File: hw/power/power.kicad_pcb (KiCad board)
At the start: 4 copper layers, 83.1 x 46.9 mm, 51 parts, among them J1 MSTB2,5/3-GF-5,08_1776511, J2 Conn_02x06, Q1 BSP315P, U1 LM5122, U2 TPS54560, U3 AMS1117-3.3

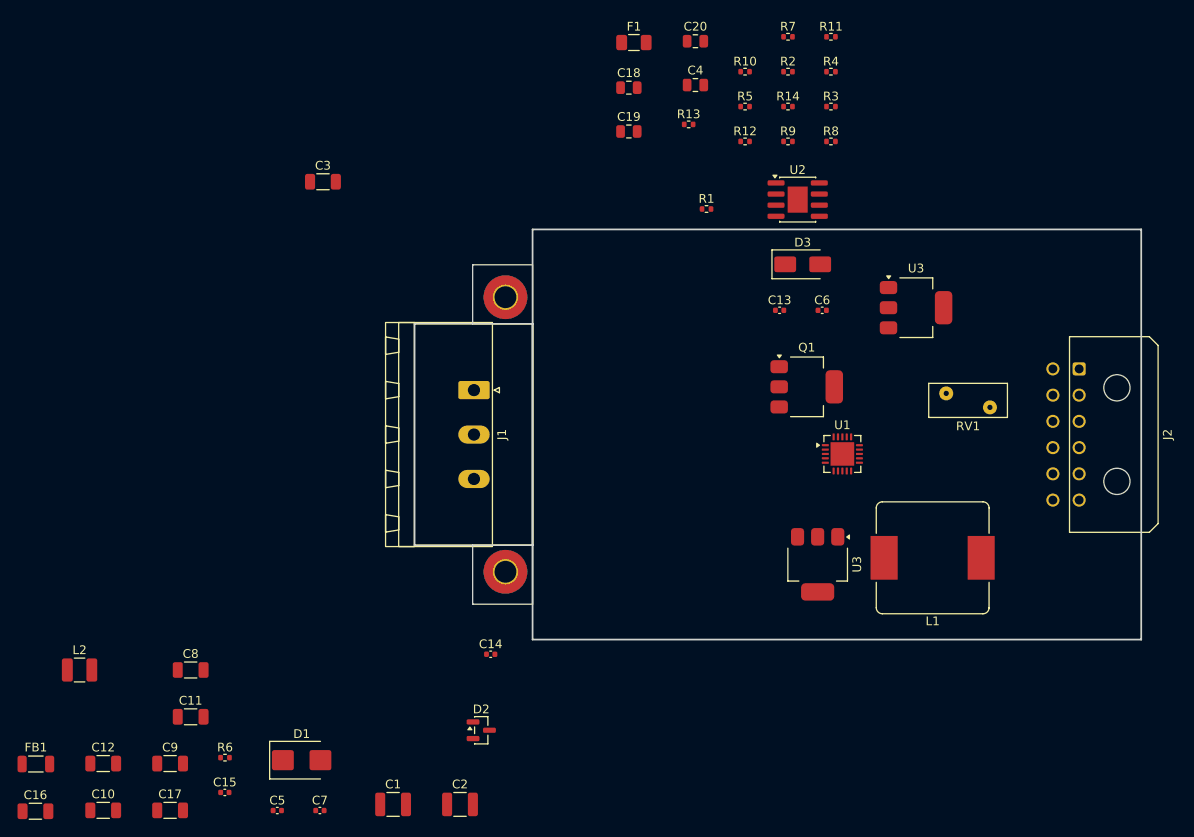
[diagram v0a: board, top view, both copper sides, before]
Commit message: s5: digital/power split, Mini-Fit interconnect, front-panel light guide
Land the board split and everything that followed from it:

- Move all switching (input protection, LM5122 boost, TPS54560 buck,
  3V3 LDO) to the power board; the core board receives finished rails.
- Board-to-board interconnect reduced to 8 pins: VBUS x2 + GND x2 +
  VIN_24V + VDD_5V + VDD_3V3 + MAIN_EN. Core J9 = Molex Mini-Fit Jr
  5569-08A1 2x4 right-angle header (serviceable, unplugs); power J2 =
  8-hole solder field (16AWG stripped ends, 1.7mm drill). Mate is an
  off-the-shelf Mini-Fit Versa 16AWG/9A cable assembly. Pin->net maps
  verified identical between the two boards.
- Front-panel status: Mentor 1278.1004 4-way bargraph light guide with
  Osram Mini TOPLED LEDs (green/yellow/orange/red), driven from the
  STM32 supervisor with PWM breathing; frees T113 PB7/PE4.
- PE: power-board input earth bonded to 4x M3_PE chassis mounting
  holes; the single GND<->PE bond stays on the core board.
- New footprints (light guide, Osram LED, 8-way solder field),
  per-board fp-lib-tables, and local vendor-3d models (${KIPRJMOD}).
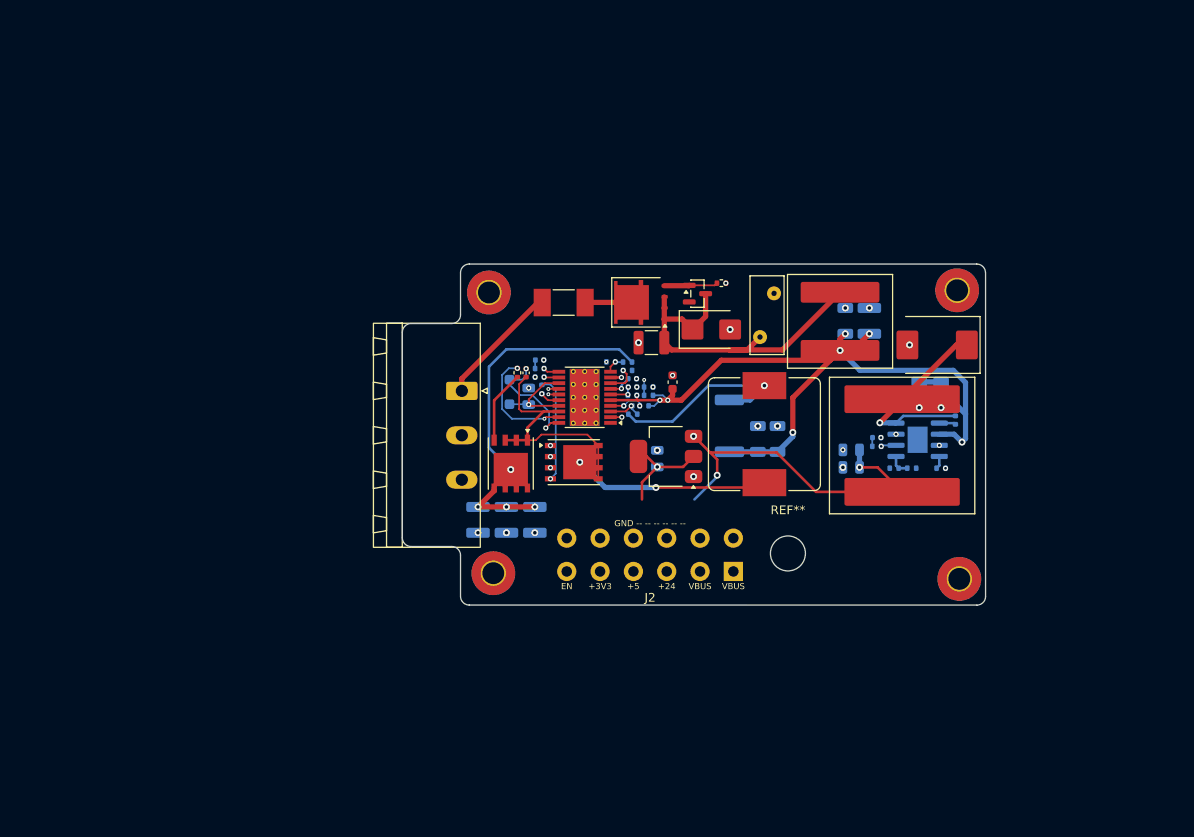
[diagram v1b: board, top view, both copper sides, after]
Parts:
- removed the J1 at (114.4, 90.7)
- removed the U3 at (164.9, 81.3)
- removed the U3 at (153.7, 110.7)
- added C21: 10uF, Capacitor_SMD:C_0805_2012Metric, B.Cu at (135.4, 98.6)
- added D4: PMEG10010ELR-QX, Diode_SMD:D_SOD-123F, B.Cu at (118.5, 90.9)
- added L1: 22uH, Inductor_SMD:L_Bourns_SRP1245A, F.Cu at (147.6, 95.8)
- added PWR_MH3: MountingHole_2.5mm_Pad_TopBottom, MountingHole:MountingHole_2.5mm_Pad_TopBottom, F.Cu at (169.7, 79.3)
- added PWR_MH4: MountingHole_2.5mm_Pad_TopBottom, MountingHole:MountingHole_2.5mm_Pad_TopBottom, F.Cu at (169.9, 112.3)
- added Q2: BSC057N08NS3G, Package_SO:PowerPAK_SO-8_Single, F.Cu at (125.8, 99.0)
- added Q3: BSC057N08NS3G, Package_SO:PowerPAK_SO-8_Single, F.Cu at (118.6, 99.1)
- added R15: 100k, Resistor_SMD:R_0402_1005Metric, B.Cu at (167.8, 99.7)
- added R16: 24.9k, Resistor_SMD:R_0402_1005Metric, B.Cu at (160.5, 97.2)
- added R17: 52.3k, Resistor_SMD:R_0402_1005Metric, B.Cu at (162.5, 99.7)
- added R18: 10k, Resistor_SMD:R_0402_1005Metric, B.Cu at (164.5, 99.7)
- added REF**: MountingHole_4mm, MountingHole:MountingHole_4mm, F.Cu at (150.3, 109.4)
- added RS: R_5m_2W, Resistor_SMD:R_2512_6332Metric, B.Cu at (143.6, 94.8)
- added U3: AMS1117-3.3, Package_TO_SOT_SMD:SOT-223-3_TabPin2, F.Cu at (136.4, 98.3)
- C10: value 10uF -> 10uF/100V; footprint Capacitor_SMD:C_1206_3216Metric -> Capacitor_SMD:C_1210_3225Metric; moved to B.Cu
- C11, C12: value 22uF -> 10uF/100V; footprint Capacitor_SMD:C_1206_3216Metric -> Capacitor_SMD:C_1210_3225Metric; moved to B.Cu
- C13, C14: value 100nF -> 22uF/63V; footprint Capacitor_SMD:C_0402_1005Metric -> Capacitor_SMD:C_1206_3216Metric; moved to B.Cu
- C15: value 15nF -> 100nF; moved to B.Cu
- C16: value 2.2uF -> 15nF; footprint Capacitor_SMD:C_1206_3216Metric -> Capacitor_SMD:C_0402_1005Metric; moved to B.Cu
- C17, C19, C2, C3, C6, C7, R7, U2: moved to B.Cu
- C18: value 22uF -> 2.2uF; footprint Capacitor_SMD:C_0805_2012Metric -> Capacitor_SMD:C_1206_3216Metric; moved to B.Cu
- C20: value 10uF -> 22uF; moved to B.Cu
- C4: value 4.7uF -> 1uF; footprint Capacitor_SMD:C_0805_2012Metric -> Capacitor_SMD:C_0603_1608Metric
- C5: value 100nF -> 4.7uF; footprint Capacitor_SMD:C_0402_1005Metric -> Capacitor_SMD:C_0805_2012Metric; moved to B.Cu
- C8: value 10uF -> 100pF; footprint Capacitor_SMD:C_1206_3216Metric -> Capacitor_SMD:C_0402_1005Metric; moved to B.Cu
- C9: value 10uF -> 100nF; footprint Capacitor_SMD:C_1206_3216Metric -> Capacitor_SMD:C_0402_1005Metric
- D1: value SMBJ30A -> SMBJ33A
- D3: value SS54 -> SS56; footprint Diode_SMD:D_SMA -> Diode_SMD:D_SMC
- F1: value Fuse_2A_TL -> Fuse_12A_TL_0452012; footprint Fuse:Fuse_1206_3216Metric -> Fuse:Fuse_Littelfuse-NANO2-451_453
- FB1: value BLM31PG601SN1 -> 2.2uH XAL1010-222MED Isat34A DCR2.8mR (LCSC C5125746); footprint Inductor_SMD:L_1206_3216Metric -> Inductor_SMD:L_Coilcraft_XAL1010-XXX
- J1: renamed from L1; value 22uH -> MSTB2,5/3-GF-5,08_1776511; footprint Inductor_SMD:L_Bourns_SRP1245A -> Connector_Phoenix_MSTB:PhoenixContact_MSTB_2,5_3-GF-5,08_1x03_P5.08mm_Horizontal_ThreadedFlange
- J2: value Conn_02x06 -> PowerCable_12way; footprint Connector_Molex:Molex_Micro-Fit_3.0_43045-1200_2x06_P3.00mm_Horizontal -> power:PowerCable_12way_SolderField
- L2: footprint Inductor_SMD:L_1210_3225Metric -> Inductor_SMD:L_Coilcraft_XAL1510-333
- Q1: value BSP315P -> SQJ409EP P-ch 40V 7mR (LCSC C727776); footprint Package_TO_SOT_SMD:SOT-223-3_TabPin2 -> Package_SO:PowerPAK_SO-8L_Single
- R10, R9: value 100k -> 100R; moved to B.Cu
- R11: value 13k -> 2.2R; moved to B.Cu
- R12: value 24.9k -> 2.2R
- R13: value 52.3k -> 100k; moved to B.Cu
- R14: value 10k -> 13k; moved to B.Cu
- R2: value 45.3k -> 100k; moved to B.Cu
- R3: value 100k -> 6.8k; moved to B.Cu
- R4: value 6.8k -> 45.3k; moved to B.Cu
- R5: value 33k -> 440k; moved to B.Cu
- R6: value 440k -> 10k; moved to B.Cu
- R8: value 10k -> 40.2k; moved to B.Cu
- U1: footprint Package_DFN_QFN:QFN-20-1EP_4x4mm_P0.5mm_EP2.7x2.7mm -> Package_SO:HTSSOP-20-1EP_4.4x6.5mm_P0.65mm_EP3.4x6.5mm_ThermalVias
- moved C16 105.3 mm to (160.5, 96.2)
- moved FB1 105.0 mm to (156.3, 82.9), turned to -90 degrees
- moved C17 98.0 mm to (165.3, 91.3), turned to -90 degrees
- moved L2 97.5 mm to (163.4, 97.1), turned to -90 degrees
- moved C15 93.8 mm to (169.5, 94.2), turned to 90 degrees
- moved C2 72.4 mm to (159.6, 82.8), turned to 90 degrees
- moved D1 68.0 mm to (141.5, 83.8)
- moved R6 63.2 mm to (130.1, 87.5), turned to 180 degrees
- moved C3 61.8 mm to (156.9, 82.8), turned to 90 degrees
- moved C1 60.5 mm to (134.7, 85.3), turned to 180 degrees
- moved C9 60.4 mm to (120.4, 88.8), turned to -90 degrees
- moved C10 59.5 mm to (121.4, 105.6), turned to -90 degrees
- moved C8 58.4 mm to (132.0, 92.5)
- moved C7 57.3 mm to (121.9, 87.3)
- moved J1 57.1 mm to (113.0, 90.8), turned to -90 degrees
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- renumbered PWR_MH1 to PWR_MH2
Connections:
- C11 pad 1: VIN_24V -> VBUS_54V
- C12 pad 1: VIN_24V -> VBUS_54V
- C13 pad 1: BOOT -> VIN_24V
- C13 pad 2: SW_NODE -> GND
- C14 pad 1: SS_TR -> VIN_24V
- C15 pad 1: COMP_MID -> BOOT
- C15 pad 2: GND -> SW_NODE
- C16 pad 1: VIN_24V -> COMP_MID
- C18 pad 1: VDD_5V -> VIN_24V
- C20 pad 1: VDD_3V3 -> VDD_5V
- C4 pad 1: BOOST_VCC -> VIN_24V
- C5 pad 1: BST_BOOST -> BOOST_VCC
- C5 pad 2: BOOST_SW -> GND
- C8 pad 1: VBUS_54V -> BOOST_CSP
- C8 pad 2: GND -> BOOST_CSN
- C9 pad 1: VBUS_54V -> BST_BOOST
- C9 pad 2: GND -> BOOST_SW
- D2 pad 1: VIN_FUSED -> RP_GATE
- D2 pad 2: RP_GATE -> (no net)
- D2 pad 3: (no net) -> VIN_PROT
- J1 pad 1: VIN_24V -> VIN_RAW
- J1 pad 2: BOOST_SW -> GND
- J2 pad 12: PWR_GOOD -> GND
- PWR_MH1 pad 1: (no net) -> EARTH
- PWR_MH2 pad 1: (no net) -> EARTH
- Q1 pad 1: RP_GATE -> VIN_PROT
- Q1 pad 3: VIN_FUSED -> VIN_PROT
- R10 pad 1: VIN_24V -> L_IN
- R10 pad 2: MAIN_EN -> BOOST_CSN
- R11 pad 1: MAIN_EN -> BOOST_LO
- R11 pad 2: GND -> QL_GATE
- R12 pad 1: COMP -> BOOST_HO
- R12 pad 2: COMP_MID -> QH_GATE
- R13 pad 1: VDD_5V -> VIN_24V
- R13 pad 2: FB_5V -> MAIN_EN
- R14 pad 1: FB_5V -> MAIN_EN
- R2 pad 1: BOOST_RT -> VIN_24V
- R2 pad 2: GND -> BOOST_UVLO
- R3 pad 1: VIN_24V -> BOOST_UVLO
- R3 pad 2: BOOST_UVLO -> GND
- R4 pad 1: BOOST_UVLO -> BOOST_RT
- R5 pad 1: BOOST_ILIM -> VBUS_54V
- R5 pad 2: GND -> BOOST_FB
- R6 pad 1: VBUS_54V -> BOOST_FB
- R6 pad 2: BOOST_FB -> GND
- R7 pad 1: BOOST_FB -> BOOST_COMP
- R7 pad 2: GND -> BOOST_COMP_MID
- R8 pad 1: BOOST_COMP -> BOOST_SLOPE
- R8 pad 2: BOOST_COMP_MID -> GND
- R9 pad 2: PWR_GOOD -> BOOST_CSP
- U1 pad 1: GND -> (no net)
- U1 pad 10: BOOST_VCC -> BOOST_FB
- U1 pad 11: BST_BOOST -> BOOST_COMP
- U1 pad 12: BOOST_HO -> BOOST_SLOPE
- U1 pad 13: BOOST_SW -> BOOST_VCC
- U1 pad 14: BOOST_LO -> GND
- U1 pad 16: BOOST_CSP -> BOOST_LO
- U1 pad 17: VIN_24V -> BOOST_VCC
- U1 pad 18: VIN_24V -> BOOST_SW
- U1 pad 19: PWR_GOOD -> BOOST_HO
- U1 pad 2: BOOST_ILIM -> GND
- U1 pad 20: BOOST_CSN -> BST_BOOST
- U1 pad 3: GND -> BOOST_CSN
- U1 pad 4: BOOST_FB -> BOOST_CSP
- U1 pad 5: BOOST_COMP -> VIN_24V
- U1 pad 6: BOOST_RT -> BOOST_UVLO
- U1 pad 8: GND -> BOOST_RT
- U1 pad 9: BOOST_UVLO -> GND
- U2 pad 4: SS_TR -> RT_CLK
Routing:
- net EARTH: track 0.00 -> 149.3 mm
- net VIN_24V: track 0.00 -> 112.7 mm, vias 0 -> 8
- net MAIN_EN: track 0.00 -> 67.7 mm, vias 0 -> 2
- net BOOST_SW: track 0.00 -> 50.5 mm, vias 0 -> 2
- net VDD_5V: track 0.00 -> 41.3 mm, vias 0 -> 3
- net VIN_PROT: track 0.00 -> 41.0 mm
- net VBUS_54V: track 0.00 -> 40.0 mm, vias 0 -> 4
- net SW_NODE: track 0.00 -> 22.7 mm, vias 0 -> 1
- net L_IN: track 0.00 -> 22.3 mm, vias 0 -> 1
- net VIN_RAW: track 0.00 -> 14.4 mm
- net BST_BOOST: track 0.00 -> 13.0 mm, vias 0 -> 2
- net BOOST_HO: track 0.00 -> 13.0 mm, vias 0 -> 2
- net QL_GATE: track 0.00 -> 12.3 mm, vias 0 -> 1
- net VDD_3V3: track 0.00 -> 11.7 mm, vias 0 -> 1
- net BOOST_VCC: track 0.00 -> 10.5 mm, vias 0 -> 1
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- added copper zone on In1.Cu, net GND
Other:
- board size 83.1 x 46.9 mm -> 66.7 x 39 mm

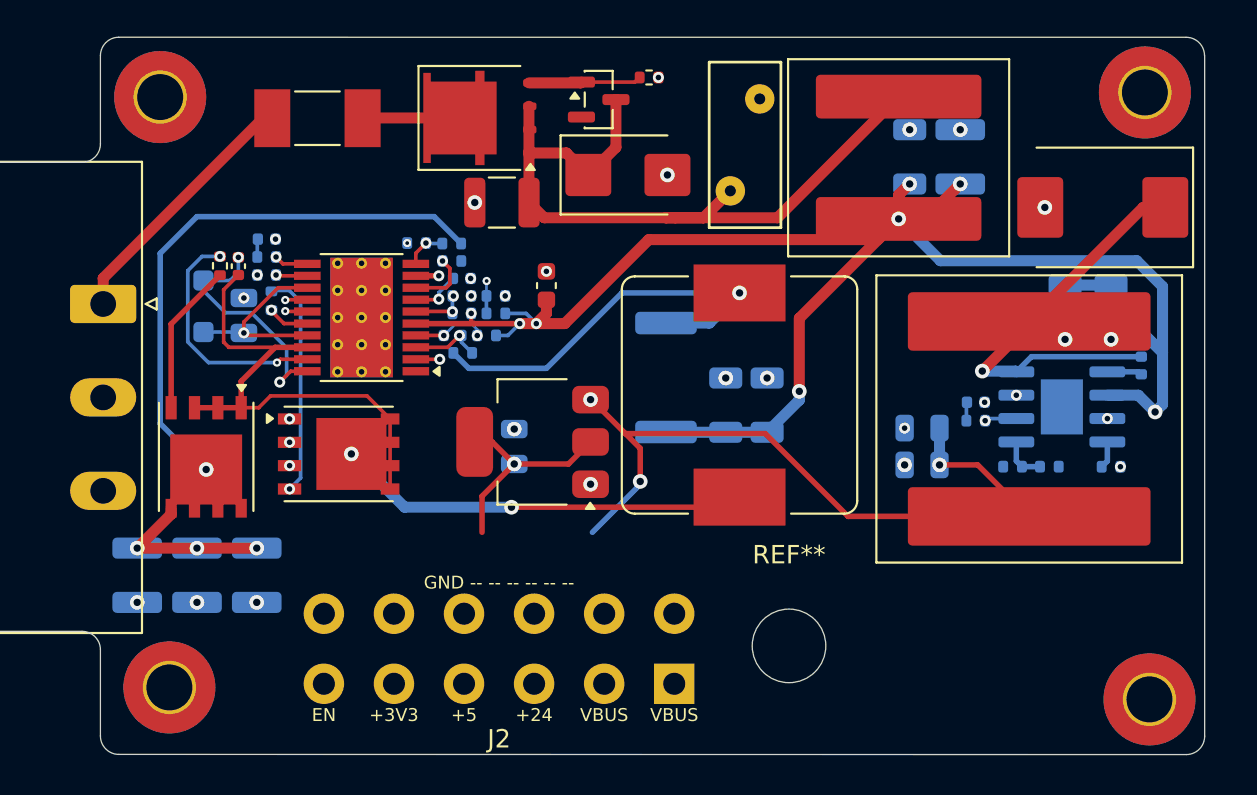
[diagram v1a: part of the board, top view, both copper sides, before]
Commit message: s5 power: point board 3D models at local vendor-3d files
Repoint L1/Q1/Q2/Q3/F1 model paths in the board to
${KIPRJMOD}/vendor-3d/*.step so the STEP export embeds them without a
netlist re-import. (A re-import will swap these footprints to the
project power.pretty copies committed in c265e82, which carry the same
paths.) Also includes KiCad's own footprint reordering from the last
edit session.
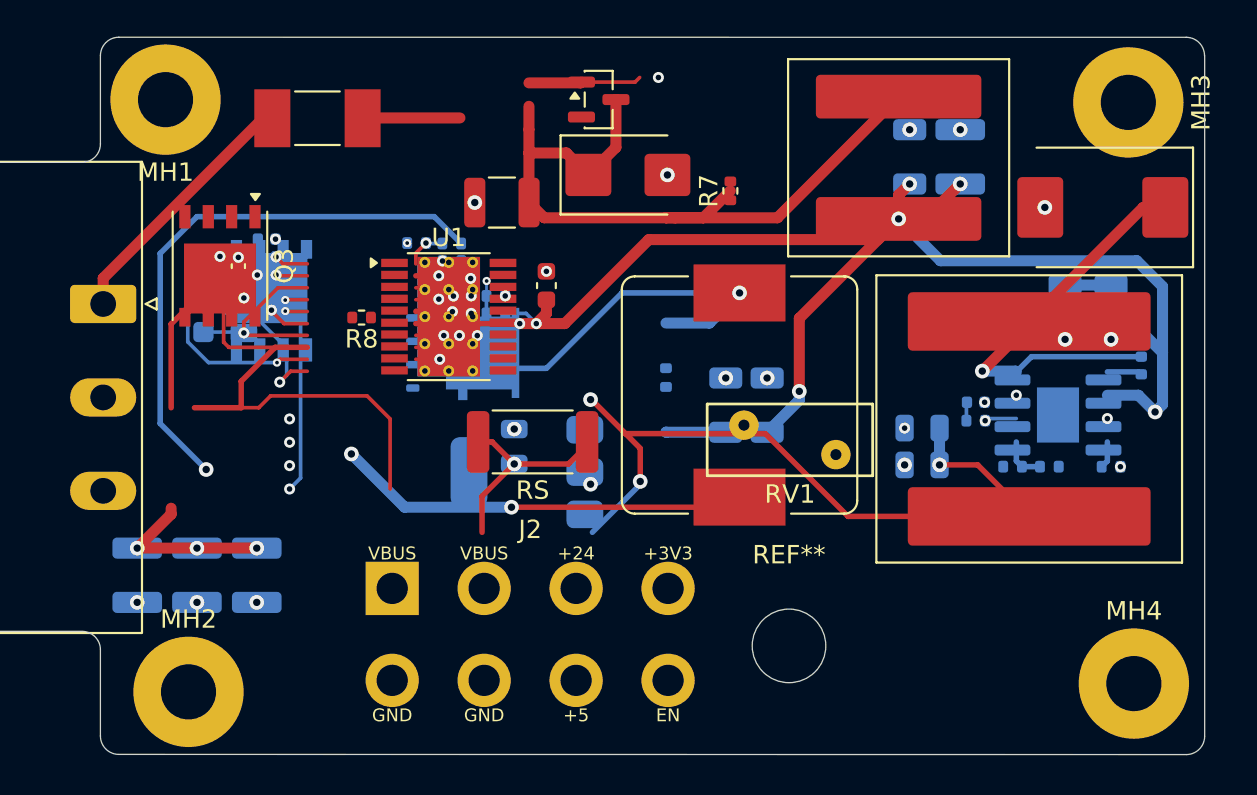
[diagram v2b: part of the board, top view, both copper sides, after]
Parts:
- removed PWR_MH1, PWR_MH2, PWR_MH3, PWR_MH4: MountingHole_2.5mm_Pad_TopBottom, MountingHole:MountingHole_2.5mm_Pad_TopBottom
- added RV1: MOV_S14K30_DNP, Varistor:RV_Disc_D9mm_W3.9mm_P5mm, F.Cu at (147.8, 97.4)
- added U1: LM5122, Package_SO:HTSSOP-20-1EP_4.4x6.5mm_P0.65mm_EP3.4x6.5mm_ThermalVias, F.Cu at (131.8, 91.5)
- added U2: TPS54560, Package_SO:SOIC-8-1EP_3.9x4.9mm_P1.27mm_EP2.29x3mm, B.Cu at (164.9, 96.8)
- added U3: AMS1117-3.3, Package_TO_SOT_SMD:SOT-223-3_TabPin2, B.Cu at (136.1, 100.0)
- J2: value PowerCable_12way -> PowerCable_8way; footprint power:PowerCable_12way_SolderField -> power:PowerCable_8way_SolderField
- MH1: renamed from Q1; value SQJ409EP P-ch 40V 7mR (LCSC C727776) -> MountingHole_M3_PE; footprint Package_SO:PowerPAK_SO-8L_Single -> MountingHole:MountingHole_3mm_Pad
- MH2: renamed from Q2; value BSC057N08NS3G -> MountingHole_M3_PE; footprint Package_SO:PowerPAK_SO-8_Single -> MountingHole:MountingHole_3mm_Pad
- MH3: renamed from Q3; value BSC057N08NS3G -> MountingHole_M3_PE; footprint Package_SO:PowerPAK_SO-8_Single -> MountingHole:MountingHole_3mm_Pad
- MH4: renamed from R1; value 100k -> MountingHole_M3_PE; footprint Resistor_SMD:R_0402_1005Metric -> MountingHole:MountingHole_3mm_Pad
- Q1: renamed from R10; value 100R -> SQJ409EP P-ch 40V 7mR (LCSC C727776); footprint Resistor_SMD:R_0402_1005Metric -> Package_SO:PowerPAK_SO-8L_Single
- Q2: renamed from R11; value 2.2R -> BSC057N08NS3G; footprint Resistor_SMD:R_0402_1005Metric -> Package_SO:PowerPAK_SO-8_Single
- Q3: renamed from R12; value 2.2R -> BSC057N08NS3G; footprint Resistor_SMD:R_0402_1005Metric -> Package_SO:PowerPAK_SO-8_Single
- R10: renamed from R14; value 13k -> 100R
- R11: renamed from R15; value 100k -> 2.2R
- R12: renamed from R16; value 24.9k -> 2.2R
- R13: renamed from R17; value 52.3k -> 100k
- R14: renamed from R18; value 10k -> 13k
- R16: renamed from R3; value 6.8k -> 24.9k
- R17: renamed from R4; value 45.3k -> 52.3k
- R18: renamed from R5; value 440k -> 10k
- R2: renamed from R6; value 10k -> 100k
- R3: renamed from R7; value 10k -> 6.8k
- R4: renamed from R8; value 40.2k -> 45.3k
- R5: renamed from R9; value 100R -> 440k
- R6: renamed from RS; value R_5m_2W -> 10k; footprint Resistor_SMD:R_2512_6332Metric -> Resistor_SMD:R_0402_1005Metric
- R7: renamed from RV1; value MOV_S14K30_DNP -> 10k; footprint Varistor:RV_Disc_D9mm_W3.9mm_P5mm -> Resistor_SMD:R_0402_1005Metric
- R8: renamed from U1; value LM5122 -> 40.2k; footprint Package_SO:HTSSOP-20-1EP_4.4x6.5mm_P0.65mm_EP3.4x6.5mm_ThermalVias -> Resistor_SMD:R_0402_1005Metric
- R9: renamed from U2; value TPS54560 -> 100R; footprint Package_SO:SOIC-8-1EP_3.9x4.9mm_P1.27mm_EP2.29x3mm -> Resistor_SMD:R_0402_1005Metric
- RS: renamed from U3; value AMS1117-3.3 -> R_5m_2W; footprint Package_TO_SOT_SMD:SOT-223-3_TabPin2 -> Resistor_SMD:R_2512_6332Metric
- moved MH3 53.7 mm to (168.8, 79.8)
- moved MH4 42.2 mm to (169.1, 111.5)
- moved MH1 17.1 mm to (116.4, 79.7)
- moved J2 16.2 mm to (128.7, 106.3), turned to 0 degrees
- moved MH2 15.3 mm to (117.7, 111.9)
- renumbered R13 to R1, R2 to R15
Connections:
- J1 pad 3: EARTH -> PE
- J2 pad 2: GND -> VBUS_54V
- J2 pad 3: VBUS_54V -> VIN_24V
- J2 pad 4: GND -> VDD_3V3
- J2 pad 5: VIN_24V -> GND
- J2 pad 8: GND -> MAIN_EN
- MH1 pad 1: VIN_PROT -> PE
- MH2 pad 1: GND -> PE
- MH3 pad 1: BOOST_SW -> PE
- MH4 pad 1: RP_GATE -> PE
- Q1 pad 1: L_IN -> VIN_PROT
- Q1 pad 2: BOOST_CSN -> VIN_PROT
- Q2 pad 1: BOOST_LO -> GND
- Q2 pad 2: QL_GATE -> GND
- Q3 pad 1: BOOST_HO -> BOOST_SW
- Q3 pad 2: QH_GATE -> BOOST_SW
- R1 pad 1: VIN_24V -> RP_GATE
- R1 pad 2: MAIN_EN -> GND
- R10 pad 1: MAIN_EN -> L_IN
- R10 pad 2: GND -> BOOST_CSN
- R11 pad 1: RT_CLK -> BOOST_LO
- R11 pad 2: GND -> QL_GATE
- R12 pad 1: COMP -> BOOST_HO
- R12 pad 2: COMP_MID -> QH_GATE
- R13 pad 1: VDD_5V -> VIN_24V
- R13 pad 2: FB_5V -> MAIN_EN
- R14 pad 1: FB_5V -> MAIN_EN
- R15 pad 1: VIN_24V -> RT_CLK
- R15 pad 2: BOOST_UVLO -> GND
- R16 pad 1: BOOST_UVLO -> COMP
- R16 pad 2: GND -> COMP_MID
- R17 pad 1: BOOST_RT -> VDD_5V
- R17 pad 2: GND -> FB_5V
- R18 pad 1: VBUS_54V -> FB_5V
- R18 pad 2: BOOST_FB -> GND
- R2 pad 1: BOOST_FB -> VIN_24V
- R2 pad 2: GND -> BOOST_UVLO
- R3 pad 1: BOOST_COMP -> BOOST_UVLO
- R3 pad 2: BOOST_COMP_MID -> GND
- R4 pad 1: BOOST_SLOPE -> BOOST_RT
- R5 pad 1: VIN_24V -> VBUS_54V
- R5 pad 2: BOOST_CSP -> BOOST_FB
- R6 pad 1: VIN_24V -> BOOST_FB
- R6 pad 2: L_IN -> GND
- R7 pad 1: VIN_PROT -> BOOST_COMP
- R7 pad 2: GND -> BOOST_COMP_MID
- R8 pad 1: (no net) -> BOOST_SLOPE
- R9 pad 1: BOOT -> VIN_24V
- R9 pad 2: VIN_24V -> BOOST_CSP
- RS pad 1: GND -> VIN_24V
- RS pad 2: VDD_3V3 -> L_IN
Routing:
- net EARTH: track 149.3 -> 0.00 mm
- net PE: track 0.00 -> 139.1 mm
- net FB_5V: track 2.45 -> 33.9 mm, vias 0 -> 2
- net VBUS_54V: track 40.0 -> 9.43 mm, vias 4 -> 3
- net BOOST_RT: track 3.35 -> 0.00 mm, vias 1 -> 0
- net MAIN_EN: track 67.7 -> 70.1 mm
- net BOOST_HO: track 13.0 -> 14.7 mm, vias 2 -> 3
- net COMP: track 1.74 -> 0.00 mm, vias 1 -> 0
- net RT_CLK: track 1.71 -> 0.00 mm
- net BOOST_LO: track 2.28 -> 3.99 mm
- net VDD_3V3: vias 1 -> 2
- net QL_GATE: vias 1 -> 2
- net GND: vias 35 -> 30
- net COMP_MID: vias 0 -> 1
- net BOOST_UVLO: vias 2 -> 3
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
